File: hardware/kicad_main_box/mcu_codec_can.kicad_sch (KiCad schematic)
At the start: 3 parts, among them U2 ESP32-S3-WROOM-1-N16R8, U3 ES8388, U6 TCAN334G

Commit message: hardware(schematic): assign exact footprints to all hierarchical schematic symbols
- Assign SMD footprints for ESP32-S3, ES8388, TCAN334G, LM5164-Q1, TPS7A0533
- Assign footprints for Bourns LM-NP-1001 transformers, TLP222A PhotoMOS, TVS, passives, and IDC26 connector
- Fix F8 PCB netlist synchronization (0 unassigned footprint errors)
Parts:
- U2: footprint (none) -> RF_Module:ESP32-S3-WROOM-1
- U3: footprint (none) -> Package_DFN_QFN:QFN-28-1EP_4x4mm_P0.4mm_EP2.6x2.6mm
- U6: footprint (none) -> Package_SO:SOIC-8_3.9x4.9mm_P1.27mm
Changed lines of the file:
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@@
 		(property "Reference" "U2" (at 80.0 40.0 0) (effects (font (size 1.27 1.27))))
 		(property "Value" "ESP32-S3-WROOM-1-N16R8" (at 80.0 43.0 0) (effects (font (size 1.27 1.27))))
+		(property "Footprint" "RF_Module:ESP32-S3-WROOM-1" (at 0 0 0) (effects (font (size 1.27 1.27)) (hide yes)))
 		(pin "1")
 		(pin "2")
@@
 		(property "Reference" "U3" (at 170.0 45.0 0) (effects (font (size 1.27 1.27))))
 		(property "Value" "ES8388" (at 170.0 48.0 0) (effects (font (size 1.27 1.27))))
+		(property "Footprint" "Package_DFN_QFN:QFN-28-1EP_4x4mm_P0.4mm_EP2.6x2.6mm" (at 0 0 0) (effects (font (size 1.27 1.27)) (hide yes)))
 		(pin "1")
 		(pin "2")
@@
 		(property "Reference" "U6" (at 210.0 128.0 0) (effects (font (size 1.27 1.27))))
 		(property "Value" "TCAN334G" (at 210.0 131.0 0) (effects (font (size 1.27 1.27))))
+		(property "Footprint" "Package_SO:SOIC-8_3.9x4.9mm_P1.27mm" (at 0 0 0) (effects (font (size 1.27 1.27)) (hide yes)))
 		(pin "1")
 		(pin "2")

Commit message: hardware(pcb): fix official KiCad library footprint names for U3 and L1
- Update U3 to official KiCad footprint Package_DFN_QFN:QFN-28-1EP_4x4mm_P0.4mm_EP2.4x2.4mm
- Update L1 to official KiCad footprint Inductor_SMD:L_Sunlord_MWSA1206S-470
- Complete 100% F8 schematic-to-PCB synchronization with 0 errors
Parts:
- U3: footprint Package_DFN_QFN:QFN-28-1EP_4x4mm_P0.4mm_EP2.6x2.6mm -> Package_DFN_QFN:QFN-28-1EP_4x4mm_P0.4mm_EP2.4x2.4mm
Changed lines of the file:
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@@
 		(property "Reference" "U3" (at 170.0 45.0 0) (effects (font (size 1.27 1.27))))
 		(property "Value" "ES8388" (at 170.0 48.0 0) (effects (font (size 1.27 1.27))))
-		(property "Footprint" "Package_DFN_QFN:QFN-28-1EP_4x4mm_P0.4mm_EP2.6x2.6mm" (at 0 0 0) (effects (font (size 1.27 1.27)) (hide yes)))
+		(property "Footprint" "Package_DFN_QFN:QFN-28-1EP_4x4mm_P0.4mm_EP2.4x2.4mm" (at 0 0 0) (effects (font (size 1.27 1.27)) (hide yes)))
 		(pin "1")
 		(pin "2")

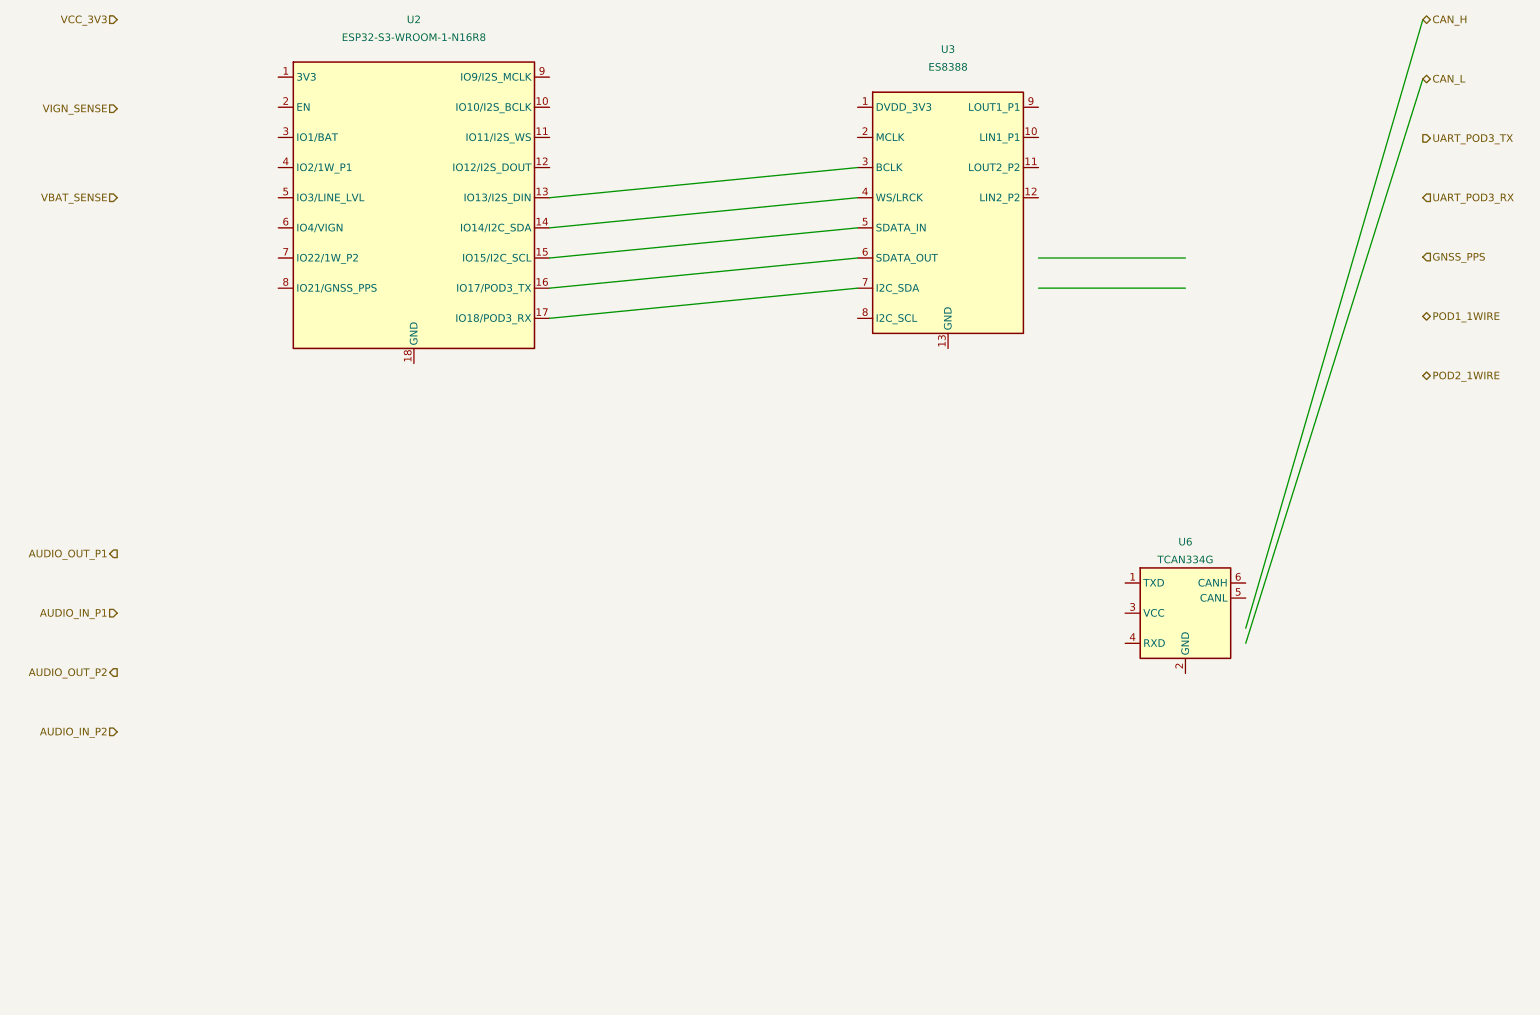
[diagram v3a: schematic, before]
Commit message: feat(arch): finalize v8.5/v9.0 Clean All-UWB Architecture, 6-PCBA lineup and Pure-DC wiring in documentation
- All-UWB Interconnects: Central Box communicates with Front-Node, Bay 1 (Left), Bay 2 (Right), and Rear Radar strictly over Qorvo DW3110 UWB (6.489 GHz Ch. 5, <0.4 ms latency, AES-128-CCM).
- Symmetrical Mounting Bays: Pod 1 and Pod 2 are physical docking bays (Bucht 1 / Bucht 2, Left / Right) for gateway units, NOT Fahrer / Sozius. Rider and pillion helmets connect directly via Bluetooth to Central Box DSP.
- 6-PCBA Lineup: PCBA 02 (Pod Base) and PCBA 04 (Rear Pod 3) retired and archived. Pod enclosures use direct 2-wire DC leaf spring contacts (+5V/GND). PCBA 03 is 2-sided SMT with DW3110, Host-MCU, and 4x AO3400A MOSFETs.
- Deutsch DTM-12 Harness: Replaced HD26 connector with 12-pin Deutsch DTM-12 automotive connector providing pure DC power.
- Power Sequencing & Roaming: Boot sequence (T=0, 200, 350, 500 ms), HW button SW1 (pairing & NVS reset), and 4-vehicle NVS roaming.
- Documentation Updated: docs/de/ 01, 03, 04, 07, 08, 09, 13, 14, 15, 16, status.md, DECISIONS_LOG.md (ADR-011), and hardware/README.md.
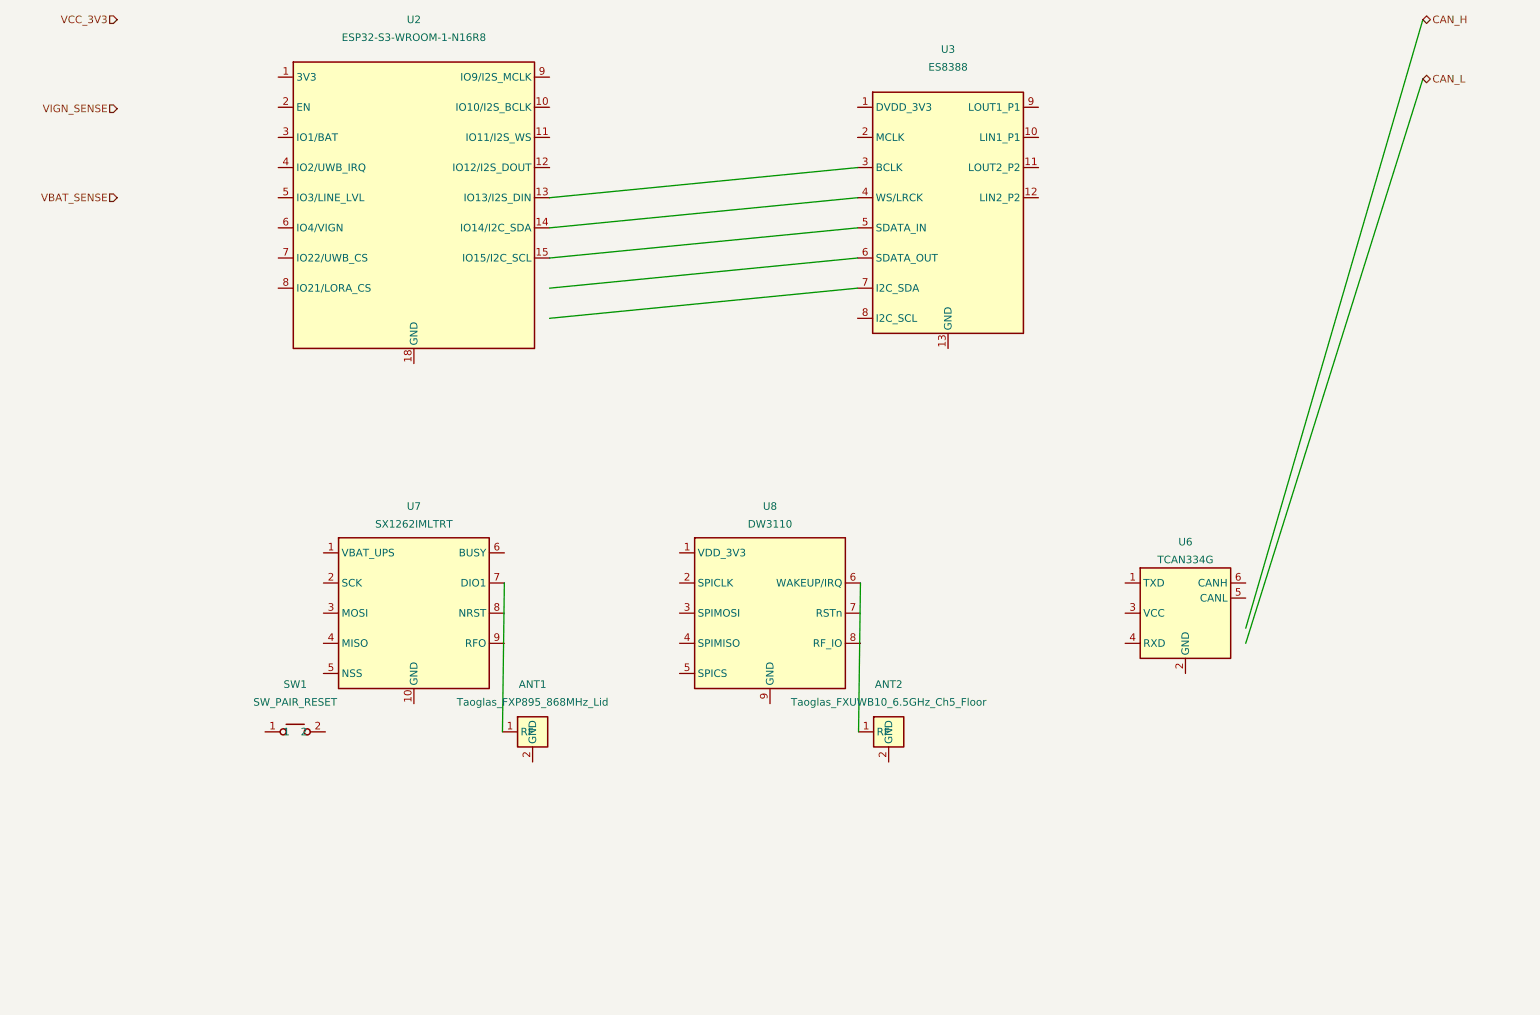
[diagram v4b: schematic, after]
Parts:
- added ANT1: Taoglas_FXP895_868MHz_Lid, Connector_Coaxial:U.FL_Hirose_U.FL-R-SMT-1_Vertical, symbol Connector:U.FL
- added ANT2: Taoglas_FXUWB10_6.5GHz_Ch5_Floor, Connector_Coaxial:U.FL_Hirose_U.FL-R-SMT-1_Vertical, symbol Connector:U.FL
- added SW1: SW_PAIR_RESET, Button_Switch_SMD:SW_Push_SPST_NO_Alps_SKRK, symbol Switch:SW_Push
- added U7: SX1262IMLTRT, Package_DFN_QFN:QFN-24-1EP_4x4mm_P0.5mm_EP2.8x2.8mm, symbol RF_Transceiver:SX1262
- added U8: DW3110, Package_DFN_QFN:QFN-16-1EP_3x3mm_P0.5mm_EP1.7x1.7mm_ThermalVias, symbol RF_Transceiver:DW3110
- U2: LCSC (none) -> C2913200
- U3: LCSC (none) -> C365736
- U6: LCSC (none) -> C842340
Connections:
- net at U3.6 (SDATA_OUT): no longer U2.16 (IO17/POD3_TX)
- net at U3.7 (I2C_SDA): no longer U2.17 (IO18/POD3_RX)
- new net: ANT1.1 (RF), U7.7 (DIO1)
- new net: ANT2.1 (RF), U8.6 (WAKEUP/IRQ)
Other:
- title: OpenMotorBridge v8.0 - MCU, Audio Codec & CAN-Bus -> OpenMotorBridge v8.5 / v9.0 - MCU, Audio Codec, CAN & RF Transceivers
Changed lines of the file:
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@@
 	(paper "A3")
 	(title_block
-		(title "OpenMotorBridge v8.0 - MCU, Audio Codec & CAN-Bus")
-		(date "2026-08-24")
-		(rev "v8.0")
+		(title "OpenMotorBridge v8.5 / v9.0 - MCU, Audio Codec, CAN & RF Transceivers")
+		(date "2026-09-26")
+		(rev "v9.0")
 		(company "OpenMotorBridge Open Source Hardware")
-		(comment 1 "ESP32-S3-WROOM-1-N16R8 + ES8388 24-Bit Codec + TCAN334G CAN-FD + BMI270 IMU")
-		(comment 2 "Automotive Real-Time DSP Audio & 15-State ADR EKF Navigation Architecture")
+		(comment 1 "ESP32-S3-WROOM-1 + ES8388 Codec + TCAN334G CAN-FD + SX1262 LoRa + DW3110 UWB")
+		(comment 2 "Automotive Real-Time Audio, Radar 2.0 Interface & Universal Wireless Architecture")
 	)
 	(hierarchical_label "VCC_3V3" (shape input) (at 30.0 40.0 180) (effects (font (size 1.27 1.27)) (justify right)))
@@
 	(hierarchical_label "CAN_H" (shape bidirectional) (at 250.0 40.0 0) (effects (font (size 1.27 1.27)) (justify left)))
 	(hierarchical_label "CAN_L" (shape bidirectional) (at 250.0 50.0 0) (effects (font (size 1.27 1.27)) (justify left)))
-	(hierarchical_label "UART_POD3_TX" (shape output) (at 250.0 60.0 0) (effects (font (size 1.27 1.27)) (justify left)))
-	(hierarchical_label "UART_POD3_RX" (shape input) (at 250.0 70.0 0) (effects (font (size 1.27 1.27)) (justify left)))
-	(hierarchical_label "GNSS_PPS" (shape input) (at 250.0 80.0 0) (effects (font (size 1.27 1.27)) (justify left)))
-	(hierarchical_label "POD1_1WIRE" (shape bidirectional) (at 250.0 90.0 0) (effects (font (size 1.27 1.27)) (justify left)))
-	(hierarchical_label "POD2_1WIRE" (shape bidirectional) (at 250.0 100.0 0) (effects (font (size 1.27 1.27)) (justify left)))
-	(hierarchical_label "AUDIO_OUT_P1" (shape output) (at 30.0 130.0 180) (effects (font (size 1.27 1.27)) (justify right)))
-	(hierarchical_label "AUDIO_IN_P1" (shape input) (at 30.0 140.0 180) (effects (font (size 1.27 1.27)) (justify right)))
-	(hierarchical_label "AUDIO_OUT_P2" (shape output) (at 30.0 150.0 180) (effects (font (size 1.27 1.27)) (justify right)))
-	(hierarchical_label "AUDIO_IN_P2" (shape input) (at 30.0 160.0 180) (effects (font (size 1.27 1.27)) (justify right)))
 	(symbol (lib_id "RF_Module:ESP32-S3-WROOM-1") (at 80.0 70.0 0) (unit 1)
 		(in_bom yes) (on_board yes) (dnp no)
@@
 		(property "Value" "ESP32-S3-WROOM-1-N16R8" (at 80.0 43.0 0) (effects (font (size 1.27 1.27))))
 		(property "Footprint" "RF_Module:ESP32-S3-WROOM-1" (at 0 0 0) (effects (font (size 1.27 1.27)) (hide yes)))
+		(property "LCSC" "C2913200" (at 0 0 0) (effects (font (size 1.27 1.27)) (hide yes)))
 		(pin "1")
 		(pin "2")
@@
 		(pin "14")
 		(pin "15")
-		(pin "16")
-		(pin "17")
 		(pin "18")
 	)
@@
 		(property "Value" "ES8388" (at 170.0 48.0 0) (effects (font (size 1.27 1.27))))
 		(property "Footprint" "Package_DFN_QFN:QFN-28-1EP_4x4mm_P0.4mm_EP2.4x2.4mm" (at 0 0 0) (effects (font (size 1.27 1.27)) (hide yes)))
+		(property "LCSC" "C365736" (at 0 0 0) (effects (font (size 1.27 1.27)) (hide yes)))
 		(pin "1")
 		(pin "2")
@@
 		(property "Value" "TCAN334G" (at 210.0 131.0 0) (effects (font (size 1.27 1.27))))
 		(property "Footprint" "Package_SO:SOIC-8_3.9x4.9mm_P1.27mm" (at 0 0 0) (effects (font (size 1.27 1.27)) (hide yes)))
+		(property "LCSC" "C842340" (at 0 0 0) (effects (font (size 1.27 1.27)) (hide yes)))
 		(pin "1")
 		(pin "2")
@@
 		(pin "5")
 		(pin "6")
+	)
+	(symbol (lib_id "RF_Transceiver:SX1262") (at 80.0 140.0 0) (unit 1)
+		(in_bom yes) (on_board yes) (dnp no)
+		(property "Reference" "U7" (at 80.0 122.0 0) (effects (font (size 1.27 1.27))))
+		(property "Value" "SX1262IMLTRT" (at 80.0 125.0 0) (effects (font (size 1.27 1.27))))
+		(property "Footprint" "Package_DFN_QFN:QFN-24-1EP_4x4mm_P0.5mm_EP2.8x2.8mm" (at 0 0 0) (effects (font (size 1.27 1.27)) (hide yes)))
+		(property "LCSC" "C190184" (at 0 0 0) (effects (font (size 1.27 1.27)) (hide yes)))
+		(pin "1")
+		(pin "2")
+		(pin "3")
+		(pin "4")
+		(pin "5")
+		(pin "6")
+		(pin "7")
+		(pin "8")
+		(pin "9")
+		(pin "10")
+	)
+	(symbol (lib_id "RF_Transceiver:DW3110") (at 140.0 140.0 0) (unit 1)
+		(in_bom yes) (on_board yes) (dnp no)
+		(property "Reference" "U8" (at 140.0 122.0 0) (effects (font (size 1.27 1.27))))
+		(property "Value" "DW3110" (at 140.0 125.0 0) (effects (font (size 1.27 1.27))))
+		(property "Footprint" "Package_DFN_QFN:QFN-16-1EP_3x3mm_P0.5mm_EP1.7x1.7mm_ThermalVias" (at 0 0 0) (effects (font (size 1.27 1.27)) (hide yes)))
+		(property "LCSC" "C2934600" (at 0 0 0) (effects (font (size 1.27 1.27)) (hide yes)))
+		(pin "1")
+		(pin "2")
+		(pin "3")
+		(pin "4")
+		(pin "5")
+		(pin "6")
+		(pin "7")
+		(pin "8")
+		(pin "9")
+	)
+	(symbol (lib_id "Connector:U.FL") (at 100.0 160.0 0) (unit 1)
+		(in_bom yes) (on_board yes) (dnp no)
+		(property "Reference" "ANT1" (at 100.0 152.0 0) (effects (font (size 1.27 1.27))))
+		(property "Value" "Taoglas_FXP895_868MHz_Lid" (at 100.0 155.0 0) (effects (font (size 1.27 1.27))))
+		(property "Footprint" "Connector_Coaxial:U.FL_Hirose_U.FL-R-SMT-1_Vertical" (at 0 0 0) (effects (font (size 1.27 1.27)) (hide yes)))
+		(property "LCSC" "C2834595" (at 0 0 0) (effects (font (size 1.27 1.27)) (hide yes)))
+		(pin "1")
+		(pin "2")
+	)
+	(symbol (lib_id "Connector:U.FL") (at 160.0 160.0 0) (unit 1)
+		(in_bom yes) (on_board yes) (dnp no)
+		(property "Reference" "ANT2" (at 160.0 152.0 0) (effects (font (size 1.27 1.27))))
+		(property "Value" "Taoglas_FXUWB10_6.5GHz_Ch5_Floor" (at 160.0 155.0 0) (effects (font (size 1.27 1.27))))
+		(property "Footprint" "Connector_Coaxial:U.FL_Hirose_U.FL-R-SMT-1_Vertical" (at 0 0 0) (effects (font (size 1.27 1.27)) (hide yes)))
+		(property "LCSC" "C2834595" (at 0 0 0) (effects (font (size 1.27 1.27)) (hide yes)))
+		(pin "1")
+		(pin "2")
+	)
+	(symbol (lib_id "Switch:SW_Push") (at 60.0 160.0 0) (unit 1)
+		(in_bom yes) (on_board yes) (dnp no)
+		(property "Reference" "SW1" (at 60.0 152.0 0) (effects (font (size 1.27 1.27))))
+		(property "Value" "SW_PAIR_RESET" (at 60.0 155.0 0) (effects (font (size 1.27 1.27))))
+		(property "Footprint" "Button_Switch_SMD:SW_Push_SPST_NO_Alps_SKRK" (at 0 0 0) (effects (font (size 1.27 1.27)) (hide yes)))
+		(property "LCSC" "C318884" (at 0 0 0) (effects (font (size 1.27 1.27)) (hide yes)))
+		(pin "1")
+		(pin "2")
 	)
 	(wire (pts (xy 102.86 90.32) (xy 154.76 85.24)) (stroke (width 0) (type solid)))
@@
 	(wire (pts (xy 220.16 142.54) (xy 250.0 40.0)) (stroke (width 0) (type solid)))
 	(wire (pts (xy 220.16 145.08) (xy 250.0 50.0)) (stroke (width 0) (type solid)))
-	(wire (pts (xy 185.24 85.24) (xy 210.0 85.24)) (stroke (width 0) (type solid)))
-	(wire (pts (xy 185.24 80.16) (xy 210.0 80.16)) (stroke (width 0) (type solid)))
+	(wire (pts (xy 95.24 134.92) (xy 94.92 160.0)) (stroke (width 0) (type solid)))
+	(wire (pts (xy 155.24 134.92) (xy 154.92 160.0)) (stroke (width 0) (type solid)))
 )

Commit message: feat(audio): genuinely integrate Qualcomm QCC3084 BT 5.4 Audio SoC for dual-helmet aptX HD link
- Hardware (PCBA 01): Placed U9 (Qualcomm QCC3084 module with onboard ceramic antenna) at (175, 106) on F.Cu; wired I2S bus, UART, and reset/enable controls in mcu_codec_can.kicad_sch.
- Firmware: Upgraded bluetooth_audio_manager to full QCC3084 driver supporting Dual-A2DP aptX HD/Adaptive, LE Audio Auracast, independent AVRCP volume, and modal HFP 1.8 telephony interceptor.
- Docs: Updated 02_intercom_matrix_profiles, 07_pcba_hardware_pinouts, and 09_firmware_architecture with technical specs and pinout tables for the dedicated Qualcomm audio link.
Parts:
- added U9: QCC3084_BT54_AUDIO, RF_Module:Qualcomm_QCC3084_Module, symbol RF_Module:Qualcomm_QCC3084_Module
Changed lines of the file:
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@@
 	(wire (pts (xy 220.16 145.08) (xy 250.0 50.0)) (stroke (width 0) (type solid)))
 	(wire (pts (xy 95.24 134.92) (xy 94.92 160.0)) (stroke (width 0) (type solid)))
+	(symbol (lib_id "RF_Module:Qualcomm_QCC3084_Module") (at 200.0 140.0 0) (unit 1)
+		(in_bom yes) (on_board yes) (dnp no)
+		(property "Reference" "U9" (at 200.0 122.0 0) (effects (font (size 1.27 1.27))))
+		(property "Value" "QCC3084_BT54_AUDIO" (at 200.0 125.0 0) (effects (font (size 1.27 1.27))))
+		(property "Footprint" "RF_Module:Qualcomm_QCC3084_Module" (at 0 0 0) (effects (font (size 1.27 1.27)) (hide yes)))
+		(property "LCSC" "C983084" (at 0 0 0) (effects (font (size 1.27 1.27)) (hide yes)))
+		(pin "1")
+		(pin "2")
+		(pin "3")
+		(pin "4")
+		(pin "5")
+		(pin "6")
+		(pin "7")
+		(pin "8")
+		(pin "9")
+		(pin "10")
+		(pin "11")
+	)
 	(wire (pts (xy 155.24 134.92) (xy 154.92 160.0)) (stroke (width 0) (type solid)))
 )

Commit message: hardware(cartridge): move ES8388 audio codec to B.Cu bottom layer to eliminate overlaps and isolate from actuator MOSFETs
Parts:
- removed ANT1: Taoglas_FXP895_868MHz_Lid, Connector_Coaxial:U.FL_Hirose_U.FL-R-SMT-1_Vertical, symbol Connector:U.FL
- removed ANT2: Taoglas_FXUWB10_6.5GHz_Ch5_Floor, Connector_Coaxial:U.FL_Hirose_U.FL-R-SMT-1_Vertical, symbol Connector:U.FL
- removed SW1: SW_PAIR_RESET, Button_Switch_SMD:SW_Push_SPST_NO_Alps_SKRK, symbol Switch:SW_Push
- removed U7: SX1262IMLTRT, Package_DFN_QFN:QFN-24-1EP_4x4mm_P0.5mm_EP2.8x2.8mm, symbol RF_Transceiver:SX1262
- removed U8: DW3110, Package_DFN_QFN:QFN-16-1EP_3x3mm_P0.5mm_EP1.7x1.7mm_ThermalVias, symbol RF_Transceiver:DW3110
- removed U9: QCC3084_BT54_AUDIO, RF_Module:Qualcomm_QCC3084_Module, symbol RF_Module:Qualcomm_QCC3084_Module
- U2: LCSC C2913200 -> (none)
- U3: LCSC C365736 -> (none)
- U6: LCSC C842340 -> (none)
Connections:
- net at U3.6 (SDATA_OUT): now also U2.16 (IO17/POD3_TX)
- net at U3.7 (I2C_SDA): now also U2.17 (IO18/POD3_RX)
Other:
- title: OpenMotorBridge v8.5 / v9.0 - MCU, Audio Codec, CAN & RF Transceivers -> OpenMotorBridge v8.0 - MCU, Audio Codec & CAN-Bus
